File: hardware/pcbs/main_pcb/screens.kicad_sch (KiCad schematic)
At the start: 22 parts, among them J1 Conn_01x02, J2 Conn_01x07, J3 Conn_01x07, J4 Conn_01x13, U1 TXB0104D, U2 TXB0104D, U3 TXB0104D

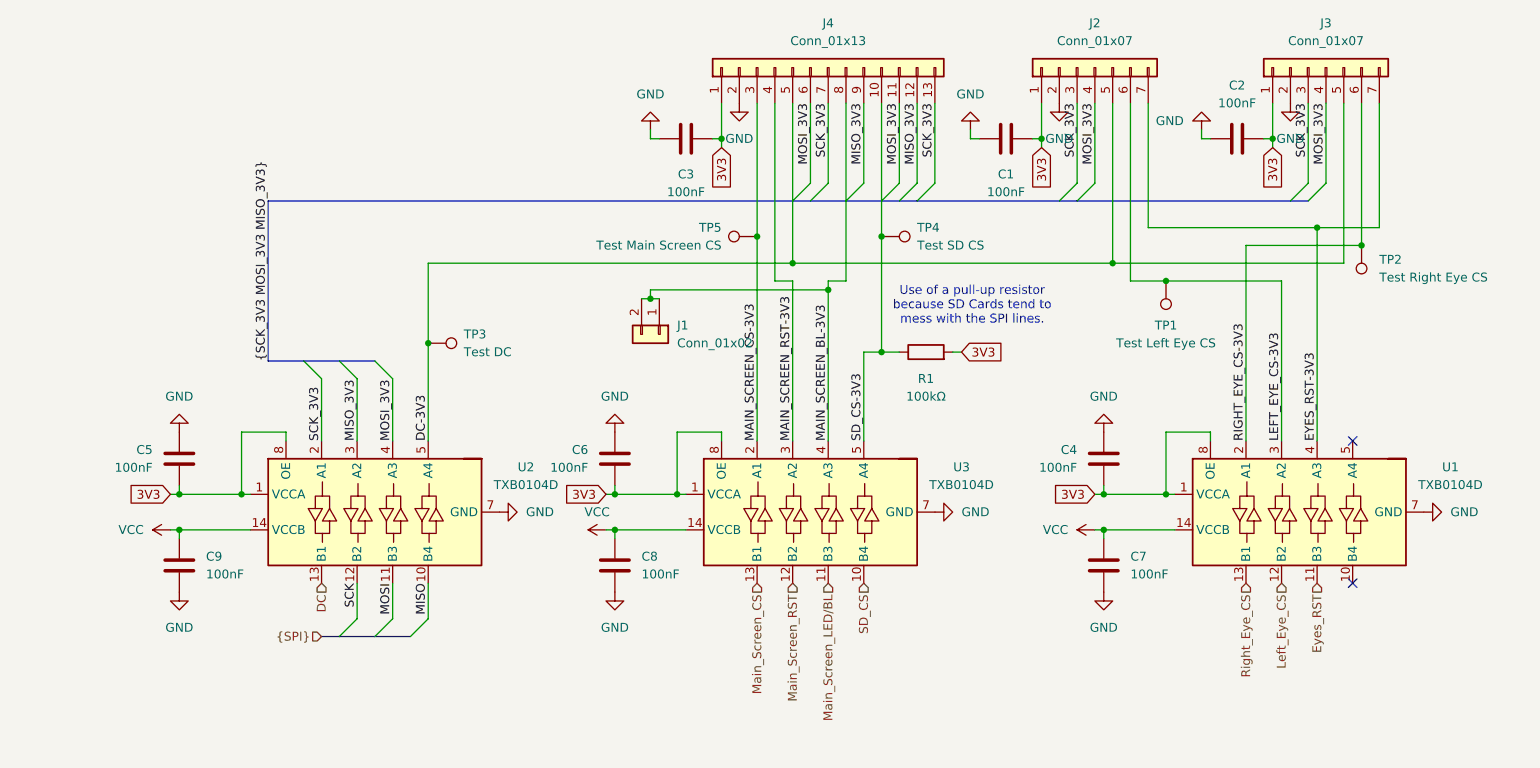
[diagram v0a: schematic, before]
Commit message: Maddie/main pcb schematic cleaning (#88)
* feat(main PCB): Reworks schematic

* feat(main PCB): Removes no longer used BL pin 01x02 header

* feat(main PCB): Fixes main PCB routing issue

* chore: Reworks main PCB schematic/PCB

* chore: Removes old csv file
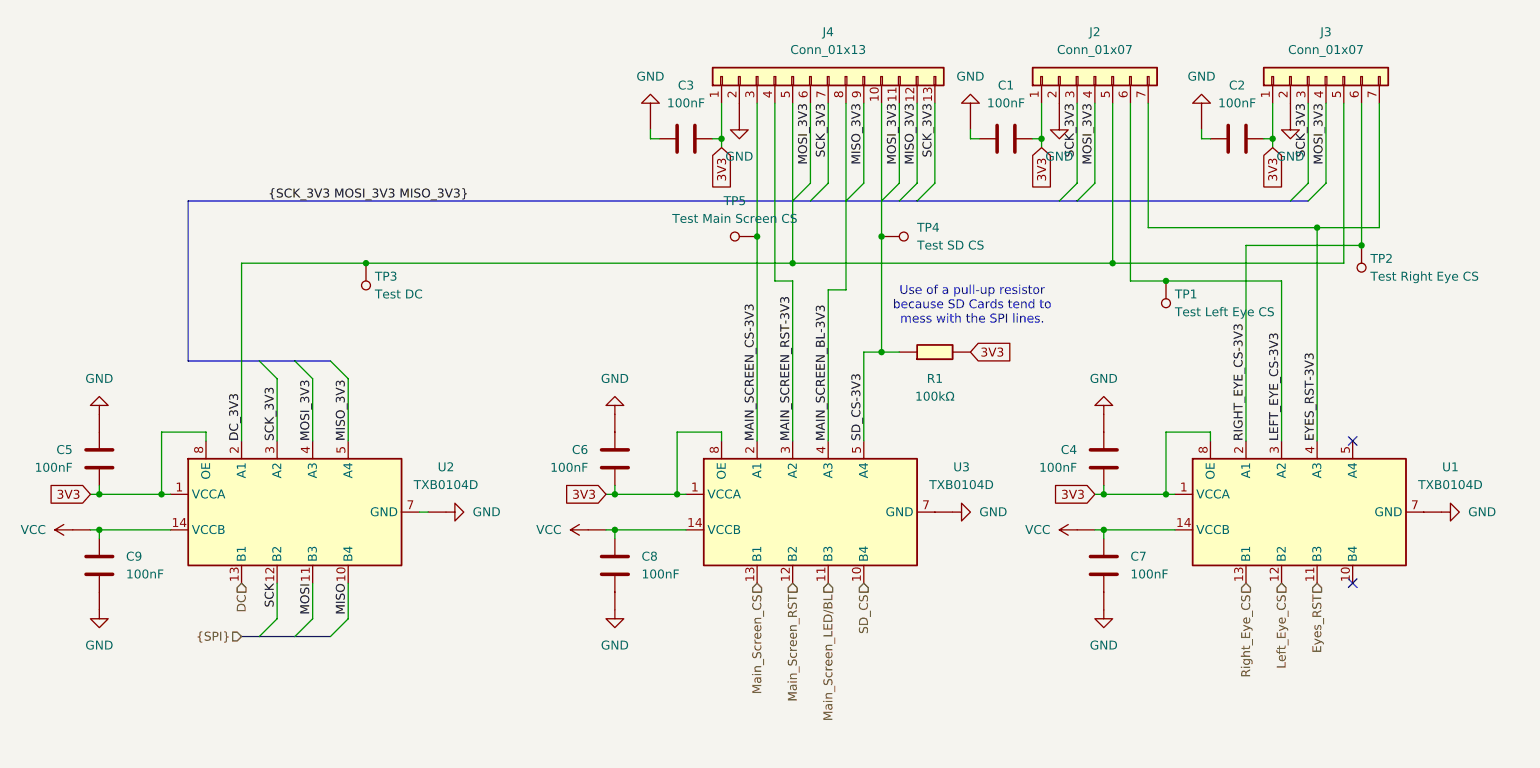
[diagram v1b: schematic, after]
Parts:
- removed J1: Conn_01x02, Lilibrary:JST XH 2 pins, symbol Connector_Generic:Conn_01x02
- C1, C2, C3, C4, C5, C6, C7, C8, C9: symbol Device:C -> Lilybrary:Capacitor
- J2, J3: symbol Connector_Generic:Conn_01x07 -> Lilybrary:Conn_01x07
- J4: symbol Connector_Generic:Conn_01x13 -> Lilybrary:Conn_01x13
- R1: symbol Device:R -> Lilybrary:Resistor
- TP1, TP2, TP3, TP4, TP5: symbol Connector:TestPoint -> Lilybrary:TestPoint
- U1, U2, U3: footprint Package_SO:SOIC-14_3.9x8.7mm_P1.27mm -> Lilibrary:SOIC-14_TXB0104DR; symbol Logic_LevelTranslator:TXB0104D -> Lilybrary:TXB0104DR
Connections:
- net MISO_3V3: now also U2.5 (A4); no longer U2.3 (A2)
- net SCK_3V3: now also U2.3 (A2); no longer U2.2 (A1)
- net DC-3V3 renamed DC_3V3
- net DC_3V3: now also U2.2 (A1); no longer U2.5 (A4)
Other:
- company: (none) -> Lily's Pad
- title: (none) -> Main PCB: Screens
- moved on the sheet: C5, C9, J2, J3, J4, TP3
